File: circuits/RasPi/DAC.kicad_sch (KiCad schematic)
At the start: 5 parts, among them J12 Conn_01x02_MountingPin, J14 Conn_01x02_MountingPin, U18 DAC_PT8211S

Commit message: シンボル・フットプリントMyLib->TomoshibiLib置き換え
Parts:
- U18: symbol MyLibrary:DAC_PT8211S -> TomoshibiLibrary:DAC_PT8211S
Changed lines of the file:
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@@
     )
   )
-  (symbol (lib_id "MyLibrary:DAC_PT8211S") (at 139.7 78.74 0) (unit 1)
+  (symbol (lib_id "TomoshibiLibrary:DAC_PT8211S") (at 139.7 78.74 0) (unit 1)
     (in_bom yes) (on_board yes) (dnp no)
     (property "Reference" "U18" (at 124.46 83.82 0)

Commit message: 更新
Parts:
- C54: footprint Capacitor_SMD:C_0603_1608Metric -> Capacitor_SMD:C_0402_1005Metric
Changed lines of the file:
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@@
       (effects (font (size 1.27 1.27)) (justify left))
     )
-    (property "Footprint" "Capacitor_SMD:C_0603_1608Metric" (at 148.2852 125.73 0)
+    (property "Footprint" "Capacitor_SMD:C_0402_1005Metric" (at 148.2852 125.73 0)
       (effects (font (size 1.27 1.27)) hide)
     )

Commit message: raspi基板回路図
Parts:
- added C64: 22uF, Capacitor_SMD:C_0805_2012Metric, symbol Device:C
- C53: value 47uF -> 22uF
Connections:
- net +5V: now also C64.1
- net GNDD: now also C64.2
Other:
- moved on the sheet: C54

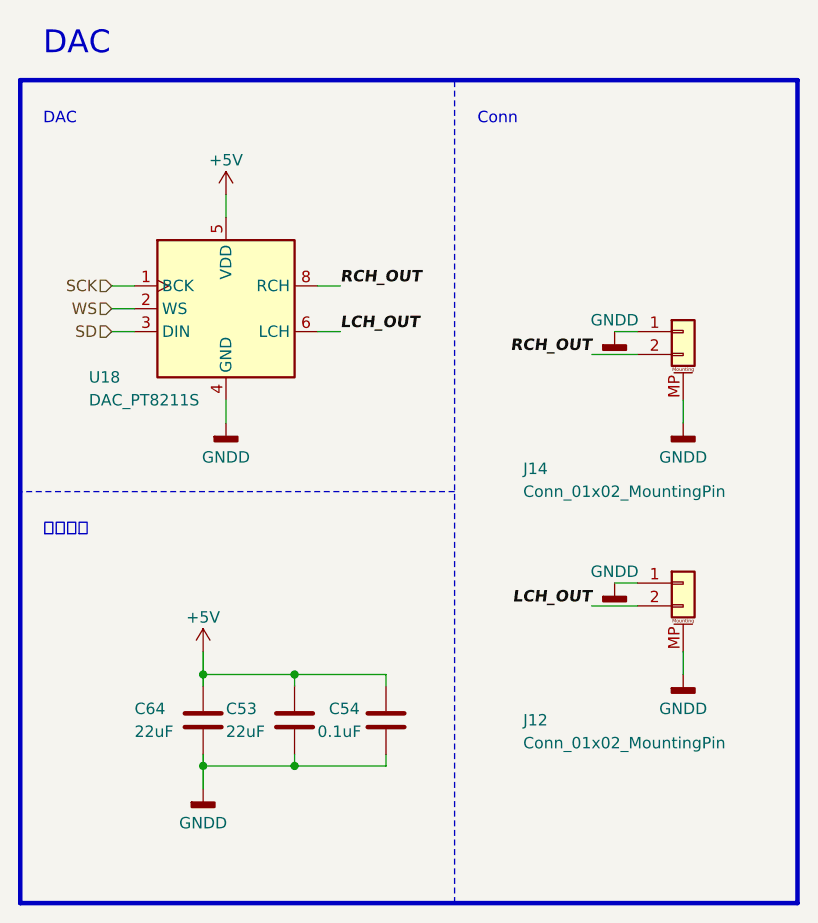
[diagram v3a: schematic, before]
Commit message: 発注第2弾
RasPi発注
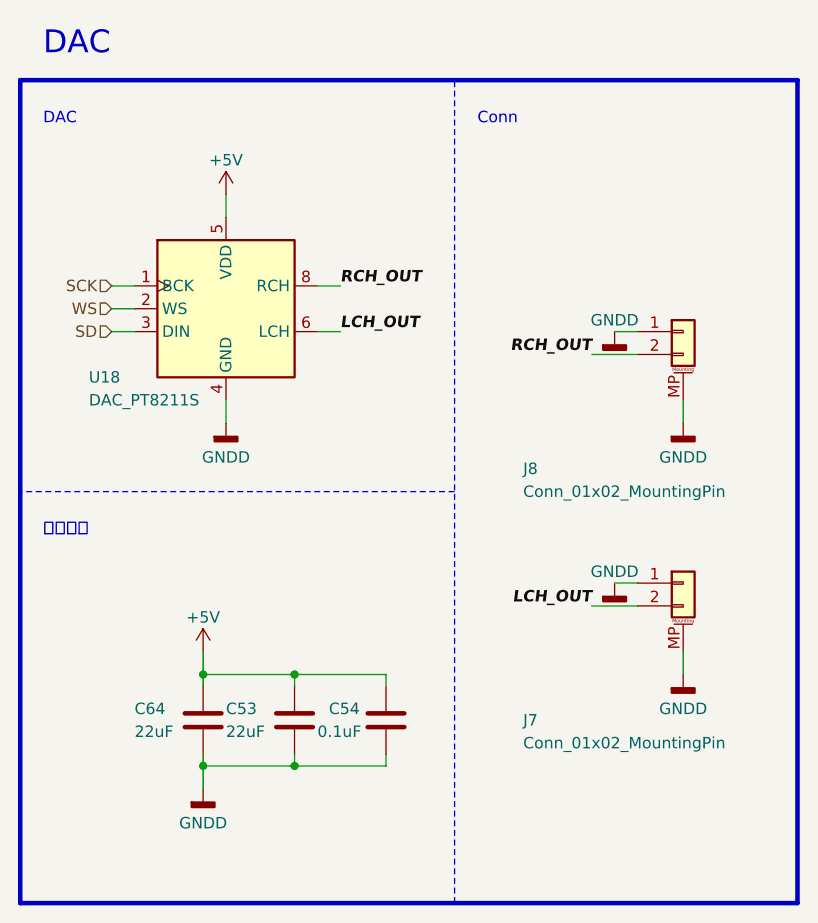
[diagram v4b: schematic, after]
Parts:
- renumbered J12 to J7, J14 to J8
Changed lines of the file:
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@@
   (symbol (lib_id "Connector_Generic_MountingPin:Conn_01x02_MountingPin") (at 190.5 78.74 0) (unit 1)
     (in_bom yes) (on_board yes) (dnp no)
-    (property "Reference" "J14" (at 172.72 93.98 0)
+    (property "Reference" "J8" (at 172.72 93.98 0)
       (effects (font (size 1.27 1.27)) (justify left))
     )
@@
       (project "RasPi"
         (path "/689a9e74-f202-4ea4-bfbb-4341f2549250/a0e6e20f-c732-4650-b515-927ea2aa6bd5/9334b424-6a5a-4e63-a4e0-775039914fa8"
-          (reference "J14") (unit 1)
+          (reference "J8") (unit 1)
         )
       )
@@
   (symbol (lib_id "Connector_Generic_MountingPin:Conn_01x02_MountingPin") (at 190.5 106.68 0) (unit 1)
     (in_bom yes) (on_board yes) (dnp no)
-    (property "Reference" "J12" (at 172.72 121.92 0)
+    (property "Reference" "J7" (at 172.72 121.92 0)
       (effects (font (size 1.27 1.27)) (justify left))
     )
@@
       (project "RasPi"
         (path "/689a9e74-f202-4ea4-bfbb-4341f2549250/a0e6e20f-c732-4650-b515-927ea2aa6bd5/9334b424-6a5a-4e63-a4e0-775039914fa8"
-          (reference "J12") (unit 1)
+          (reference "J7") (unit 1)
         )
       )
